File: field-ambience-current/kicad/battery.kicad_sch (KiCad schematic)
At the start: 22 parts, among them J9 JST PH 2.0 2-pin (LiPo Batter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, Q1 DMG2305UX P-MOS SOT-23 (USB-C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, U7 MCP73831T-2ACI/OT (LiPo Charg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, U8 TPS61089RNR (Boost LiPo→5V, 2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

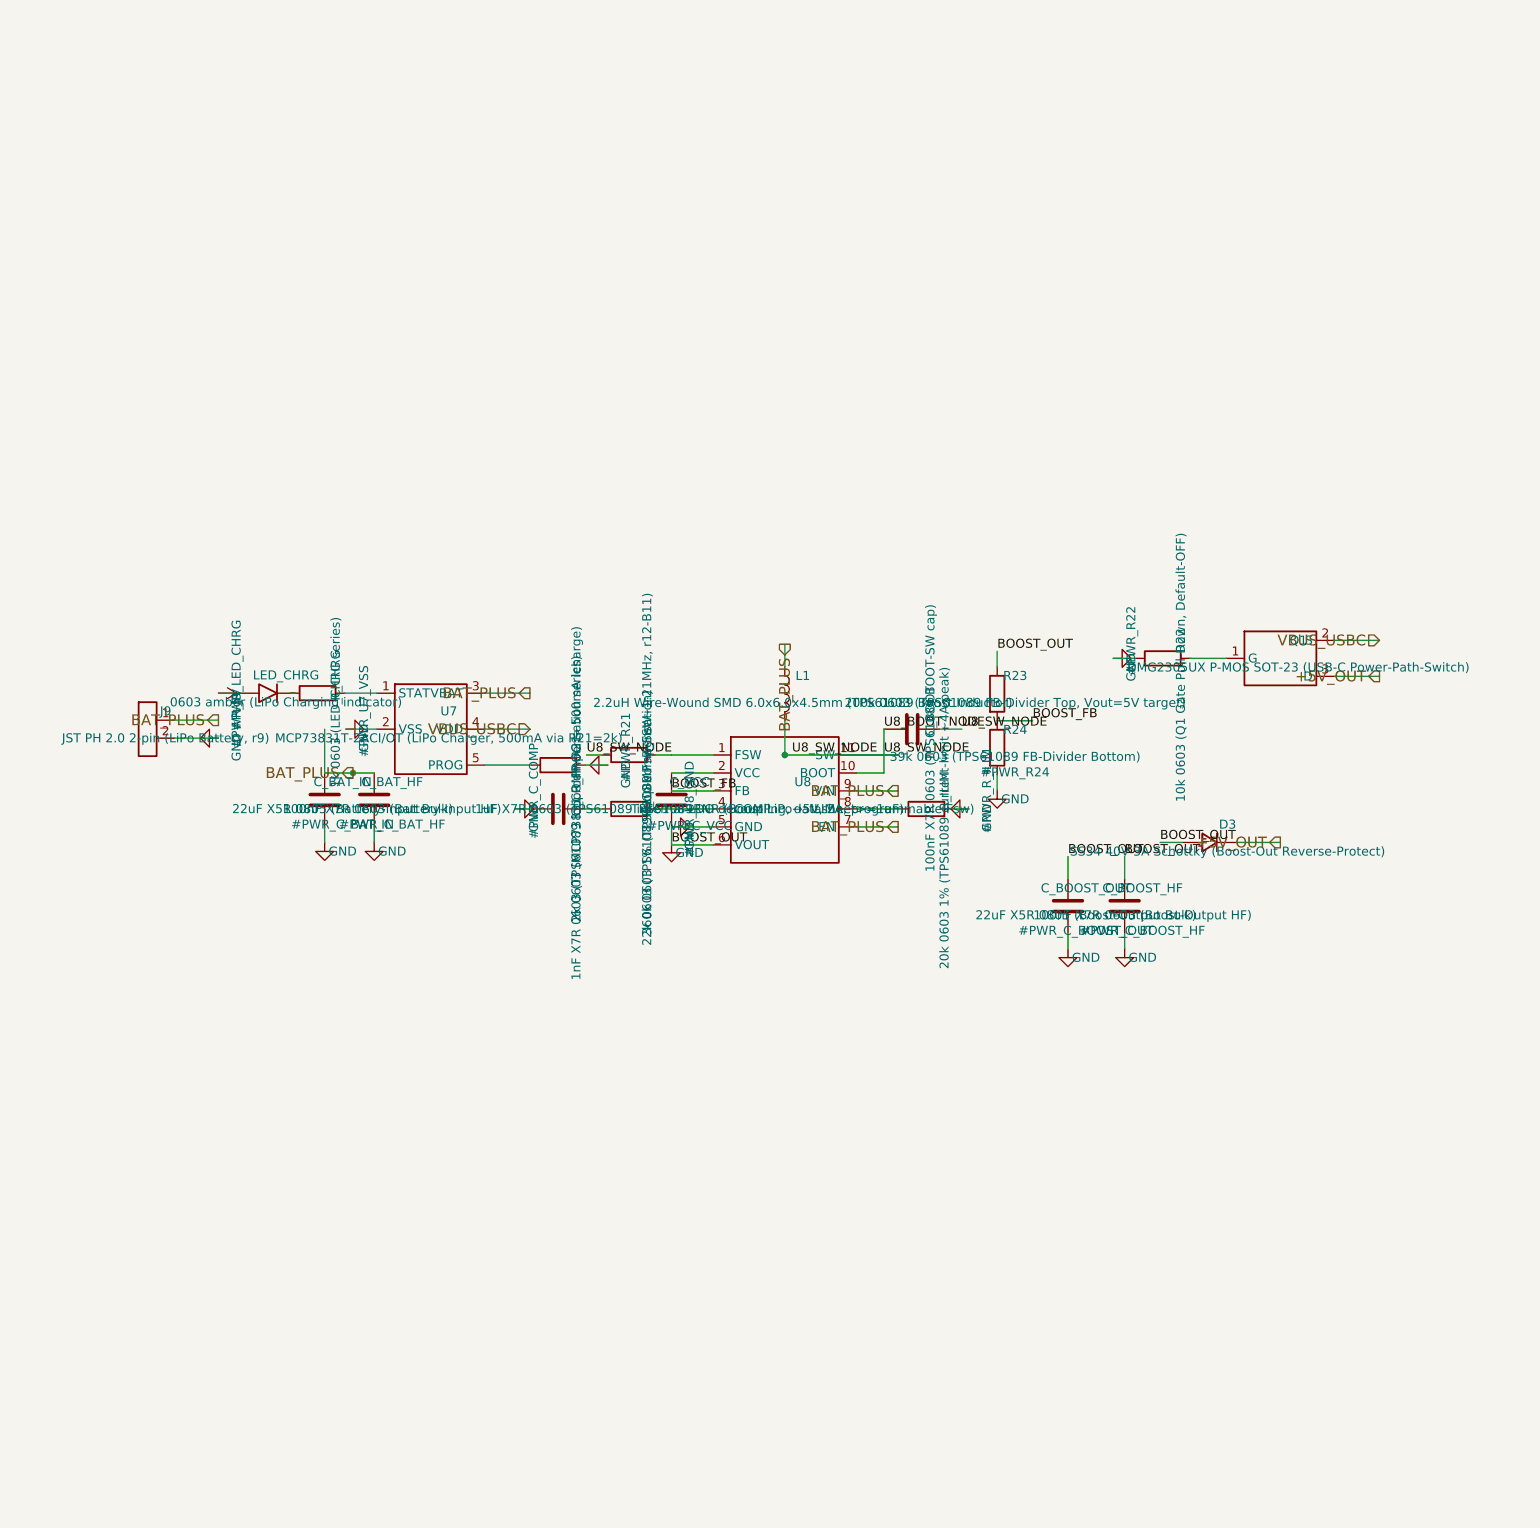
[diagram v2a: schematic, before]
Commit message: fix(power): electrical audit — 3 critical boost/power-path bugs (r18.79) (#91)
User asked for a components+connections review (no mechanics), looking for
critical errors. Systematic electrical audit of the generated schematics:
hier-label<->root-pin matching, root wiring connectivity (union-find over
wire endpoints + label-name merging), dangling nets, duplicate refdes, I2C
addresses, pull-ups, and the boost converter checked line-by-line against
the TI TPS61089 datasheet (SLVSD38C -- equations read from rendered PDF
pages, not from memory).

CRITICAL FIX 1 -- boost FB divider set the "+5V" rail to 7.43V:
R23/R24 = 200k/39k with VREF 1.212V (TI EC table) gives VOUT = 7.43V, not
5V. That would have destroyed the PAM8403 amp (5.5V abs max) and the
planned TPS22918 load switch (5.5V max) at first power-on, and overstressed
the AP7361C LDO (6V max). Fix: R23 = 121k (0603WAF1213T5E, C25809, live-
verified, 71k stock) -> VOUT = 4.97V per DS Eq. 5. (122k for exactly 5.00V
has no verifiable LCSC stock; -0.6% errs in the safe direction.)

CRITICAL FIX 2 -- R_ILIM 20k = 51.5A current limit (i.e. none):
TI Eq. 4: ILIM = 1,030,000 / R_ILIM. The generator comment claimed "20k ->
~4A peak"; the real result is 51.5A -- effectively no current limit, with
the inductor (Isat min 6.75A) unprotected under fault. Fix: R_ILIM = 174k
(0603WAF1743T5E, C22890, live-verified) -> 5.92A typ / 5.12A min (above the
~4.7A worst-case operating peak) / ~6.7A max (below Isat-min 6.75A).

CRITICAL FIX 3 -- Q1 power-path back-feed + fuse bypass:
Q1 (P-FET, S=VBUS pre-fuse, D=+5V rail, G->GND) plus power_tree exporting
the rail directly behind F1 meant: with no USB plugged in, the boost's 5V
back-fed VBUS through Q1's body diode (and in parallel through F1 -- PTC
fuses conduct both ways), pulling the gate-source negative and latching Q1
fully on. Consequences: the charger (VDD = VBUS_USBC) charged the battery
from its own boost output -- a self-discharge loop draining the battery at
~1.5x the charge cu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
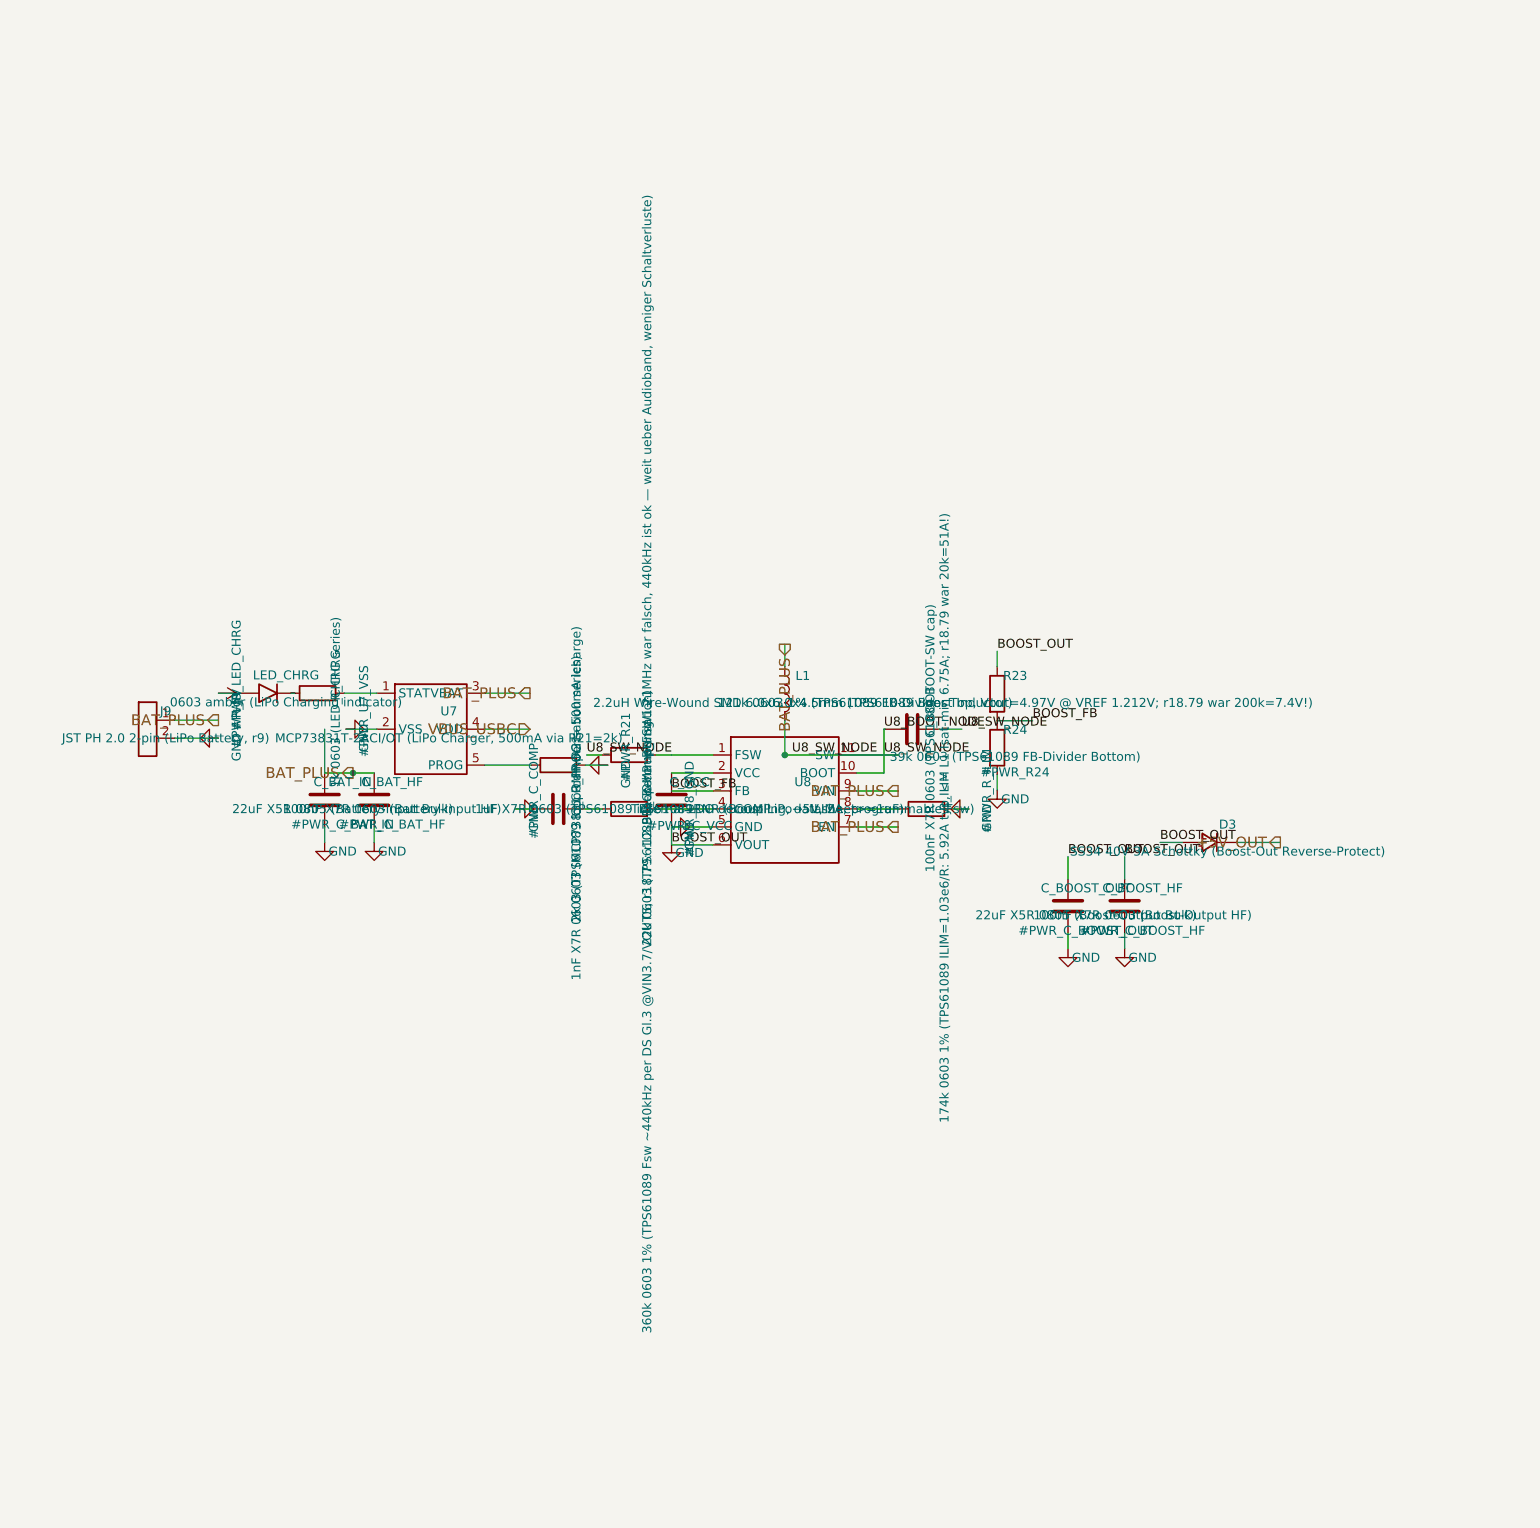
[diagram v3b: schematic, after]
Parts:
- removed Q1: DMG2305UX P-MOS SOT-23 (USB-C Power-Path-Switch), Package_TO_SOT_SMD:SOT-23, symbol Transistor_FET:DMG2305UX
- removed R22: 10k 0603 (Q1 Gate Pull-Down, Default-OFF), Resistor_SMD:R_0603_1608Metric, symbol Device:R
- R23: value 200k 0603 (TPS61089 FB-Divider Top, Vout=5V target) -> 121k 0603 1% (TPS61089 FB-Divider Top, Vout=4.97V @ VREF 1.212V; r18.79 war 200k=7.4V!); LCSC C25811 -> C25809; MPN 0603WAF2003T5E -> 0603WAF1213T5E
- R_FSW: value 360k 0603 1% (TPS61089 Fsw-Set ~1.21MHz, r12-B11) -> 360k 0603 1% (TPS61089 Fsw ~440kHz per DS Gl.3 @VIN3.7/VOUT5; r18.79: r12-B11-Behauptung 1.21MHz war falsch, 440kHz ist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
- R_ILIM: value 20k 0603 1% (TPS61089 current-limit ~4A peak) -> 174k 0603 1% (TPS61089 ILIM=1.03e6/R: 5.92A typ, <= L1 Isat-min 6.75A; r18.79 war 20k=51A!); LCSC C4184 -> C22890; MPN 0603WAF2002T5E -> 0603WAF1743T5E
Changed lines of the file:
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@@
       (property "Reference" "R_FSW" (at 120.54 81.11 0)
         (effects (font (size 1.27 1.27))))
-      (property "Value" "360k 0603 1% (TPS61089 Fsw-Set ~1.21MHz, r12-B11)" (at 120.54 84.92 0)
+      (property "Value" "360k 0603 1% (TPS61089 Fsw ~440kHz per DS Gl.3 @VIN3.7/VOUT5; r18.79: r12-B11-Behauptung 1.21MHz war falsch, 440kHz ist ok — weit ueber Audioband, weniger Schaltverluste)" (at 120.54 84.92 0)
         (effects (font (size 1.27 1.27))))
       (property "Footprint" "Resistor_SMD:R_0603_1608Metric" (at 118 83.65 0)
@@
       (property "Reference" "R23" (at 172.54 72.46 0)
         (effects (font (size 1.27 1.27))))
-      (property "Value" "200k 0603 (TPS61089 FB-Divider Top, Vout=5V target)" (at 172.54 76.27 0)
+      (property "Value" "121k 0603 1% (TPS61089 FB-Divider Top, Vout=4.97V @ VREF 1.212V; r18.79 war 200k=7.4V!)" (at 172.54 76.27 0)
         (effects (font (size 1.27 1.27))))
       (property "Footprint" "Resistor_SMD:R_0603_1608Metric" (at 170 75 0)
@@
       (property "Datasheet" "~" (at 170 75 0)
         (effects (font (size 1.27 1.27)) hide))
-      (property "MPN" "0603WAF2003T5E" (at 172.54 78.81 0)
-        (effects (font (size 1.27 1.27)) hide))
-      (property "LCSC" "C25811" (at 172.54 80.08 0)
+      (property "MPN" "0603WAF1213T5E" (at 172.54 78.81 0)
+        (effects (font (size 1.27 1.27)) hide))
+      (property "LCSC" "C25809" (at 172.54 80.08 0)
         (effects (font (size 1.27 1.27)) hide))
     (instances
@@
       (property "Reference" "R_ILIM" (at 162.54 88.73 0)
         (effects (font (size 1.27 1.27))))
-      (property "Value" "20k 0603 1% (TPS61089 current-limit ~4A peak)" (at 162.54 92.54 0)
+      (property "Value" "174k 0603 1% (TPS61089 ILIM=1.03e6/R: 5.92A typ, <= L1 Isat-min 6.75A; r18.79 war 20k=51A!)" (at 162.54 92.54 0)
         (effects (font (size 1.27 1.27))))
       (property "Footprint" "Resistor_SMD:R_0603_1608Metric" (at 160 91.27000000000001 0)
@@
       (property "Datasheet" "~" (at 160 91.27000000000001 0)
         (effects (font (size 1.27 1.27)) hide))
-      (property "MPN" "0603WAF2002T5E" (at 162.54 95.08000000000001 0)
-        (effects (font (size 1.27 1.27)) hide))
-      (property "LCSC" "C4184" (at 162.54 96.35000000000001 0)
+      (property "MPN" "0603WAF1743T5E" (at 162.54 95.08000000000001 0)
+        (effects (font (size 1.27 1.27)) hide))
+      (property "LCSC" "C22890" (at 162.54 96.35000000000001 0)
         (effects (font (size 1.27 1.27)) hide))
     (instances
@@
       (project "field_ambience"
         (path "/f6a664dc-7032-4108-a10b-e4076008e6bd" (reference "D3") (unit 1)))))
-  (symbol (lib_id "Transistor_FET:DMG2305UX") (at 210.0 70.0 0) (unit 1)
-    (in_bom yes) (on_board yes) (dnp no)
-      (property "Reference" "Q1" (at 212.54 67.46 0)
-        (effects (font (size 1.27 1.27))))
-      (property "Value" "DMG2305UX P-MOS SOT-23 (USB-C Power-Path-Switch)" (at 212.54 71.27 0)
-        (effects (font (size 1.27 1.27))))
-      (property "Footprint" "Package_TO_SOT_SMD:SOT-23" (at 210.0 70.0 0)
-        (effects (font (size 1.27 1.27)) hide))
-      (property "Datasheet" "https://www.diodes.com/assets/Datasheets/DMG2305UX.pdf" (at 210.0 70.0 0)
-        (effects (font (size 1.27 1.27)) hide))
-      (property "MPN" "DMG2305UX-7" (at 212.54 73.81 0)
-        (effects (font (size 1.27 1.27)) hide))
-      (property "LCSC" "C150470" (at 212.54 75.08 0)
-        (effects (font (size 1.27 1.27)) hide))
-    (instances
-      (project "field_ambience"
-        (path "/f6a664dc-7032-4108-a10b-e4076008e6bd" (reference "Q1") (unit 1)))))
-  (symbol (lib_id "Device:R") (at 193.38 70.0 90) (unit 1)
-    (in_bom yes) (on_board yes) (dnp no)
-      (property "Reference" "R22" (at 195.92 67.46 0)
-        (effects (font (size 1.27 1.27))))
-      (property "Value" "10k 0603 (Q1 Gate Pull-Down, Default-OFF)" (at 195.92 71.27 0)
-        (effects (font (size 1.27 1.27))))
-      (property "Footprint" "Resistor_SMD:R_0603_1608Metric" (at 193.38 70.0 0)
-        (effects (font (size 1.27 1.27)) hide))
-      (property "Datasheet" "~" (at 193.38 70.0 0)
-        (effects (font (size 1.27 1.27)) hide))
-      (property "MPN" "0603WAF1002T5E" (at 195.92 73.81 0)
-        (effects (font (size 1.27 1.27)) hide))
-      (property "LCSC" "C25804" (at 195.92 75.08 0)
-        (effects (font (size 1.27 1.27)) hide))
-    (instances
-      (project "field_ambience"
-        (path "/f6a664dc-7032-4108-a10b-e4076008e6bd" (reference "R22") (unit 1)))))
-  (symbol (lib_id "Power:GND") (at 186.38 70.0 90) (unit 1)
-    (in_bom yes) (on_board yes) (dnp no)
-      (property "Reference" "#PWR_R22" (at 188.92 67.46 0)
-        (effects (font (size 1.27 1.27))))
-      (property "Value" "GND" (at 188.92 71.27 0)
-        (effects (font (size 1.27 1.27))))
-      (property "Footprint" "" (at 186.38 70.0 0)
-        (effects (font (size 1.27 1.27)) hide))
-      (property "Datasheet" "~" (at 186.38 70.0 0)
-        (effects (font (size 1.27 1.27)) hide))
-    (instances
-      (project "field_ambience"
-        (path "/f6a664dc-7032-4108-a10b-e4076008e6bd" (reference "#PWR_R22") (unit 1)))))
   (wire (pts (xy 53.81 78.73) (xy 60 78.73))
     (stroke (width 0) (type default))
@@
     (stroke (width 0) (type default))
 )
-  (wire (pts (xy 202.38 70.0) (xy 197.38 70.0))
-    (stroke (width 0) (type default))
-)
-  (wire (pts (xy 189.57 70.0) (xy 186.38 70.0))
-    (stroke (width 0) (type default))
-)
-  (wire (pts (xy 197.19 70.0) (xy 197.38 70.0))
-    (stroke (width 0) (type default))
-)
-  (wire (pts (xy 217.62 67.46) (xy 224.0 67.46))
-    (stroke (width 0) (type default))
-)
-  (wire (pts (xy 217.62 72.54) (xy 224.0 72.54))
-    (stroke (width 0) (type default))
-)
   (junction (at 79 86.19) (diameter 0) (color 0 0 0 0)
 )
@@
     (effects (font (size 1.524 1.524)) (justify right))
 )
-  (hierarchical_label "VBUS_USBC" (shape input) (at 224.0 67.46 180)
-    (effects (font (size 1.524 1.524)) (justify right))
-)
-  (hierarchical_label "+5V_OUT" (shape output) (at 224.0 72.54 0)
-    (effects (font (size 1.524 1.524)) (justify right))
-)
